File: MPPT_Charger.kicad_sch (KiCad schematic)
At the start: 124 parts, among them J1 Solar, J2 Battery, J4 INTERFACE PORT, J6 JTAG/KEYS, J8 Micro_SD_Card_Det_Hirose_DM3AT, J9 IIC RTC, P1 USB_C_Receptacle_USB2.0_16P, Q1 CSD19505KCS, Q2 CSD19505KCS, Q3 CSD19505KCS, Q4 Si2306, Q5 MMBT3904 1A, Q6 MMBT3904 1A, Q7 Si2306, U1 ACS712, U10 ADS1015, U2 B1212S, U3 AMS1117-5.0, U4 AMS1117-3.3, U5 XL7005A, U6 XL7005A, U7 IR2104, U8 ESP32, U9 CH340G

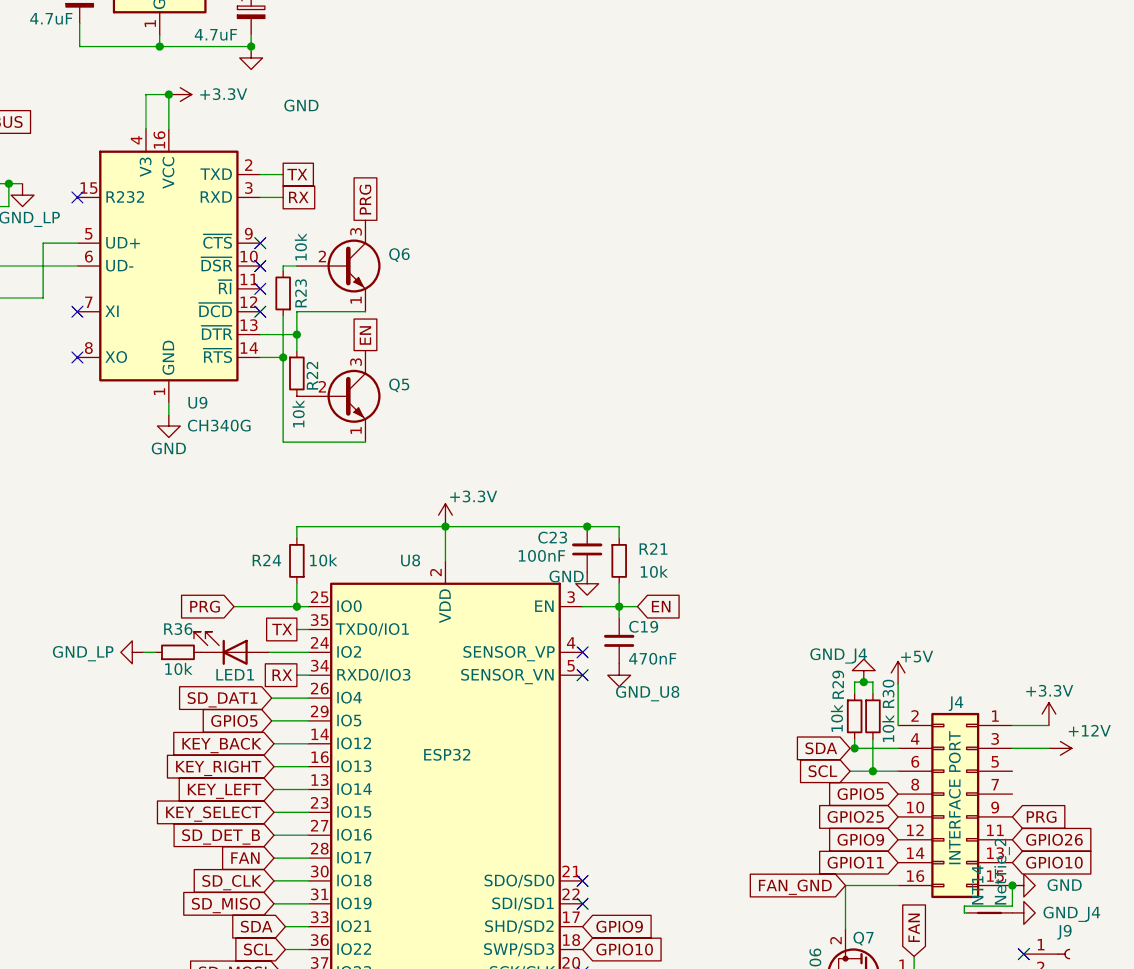
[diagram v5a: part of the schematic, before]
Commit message: RxD TxD were wrong :-(
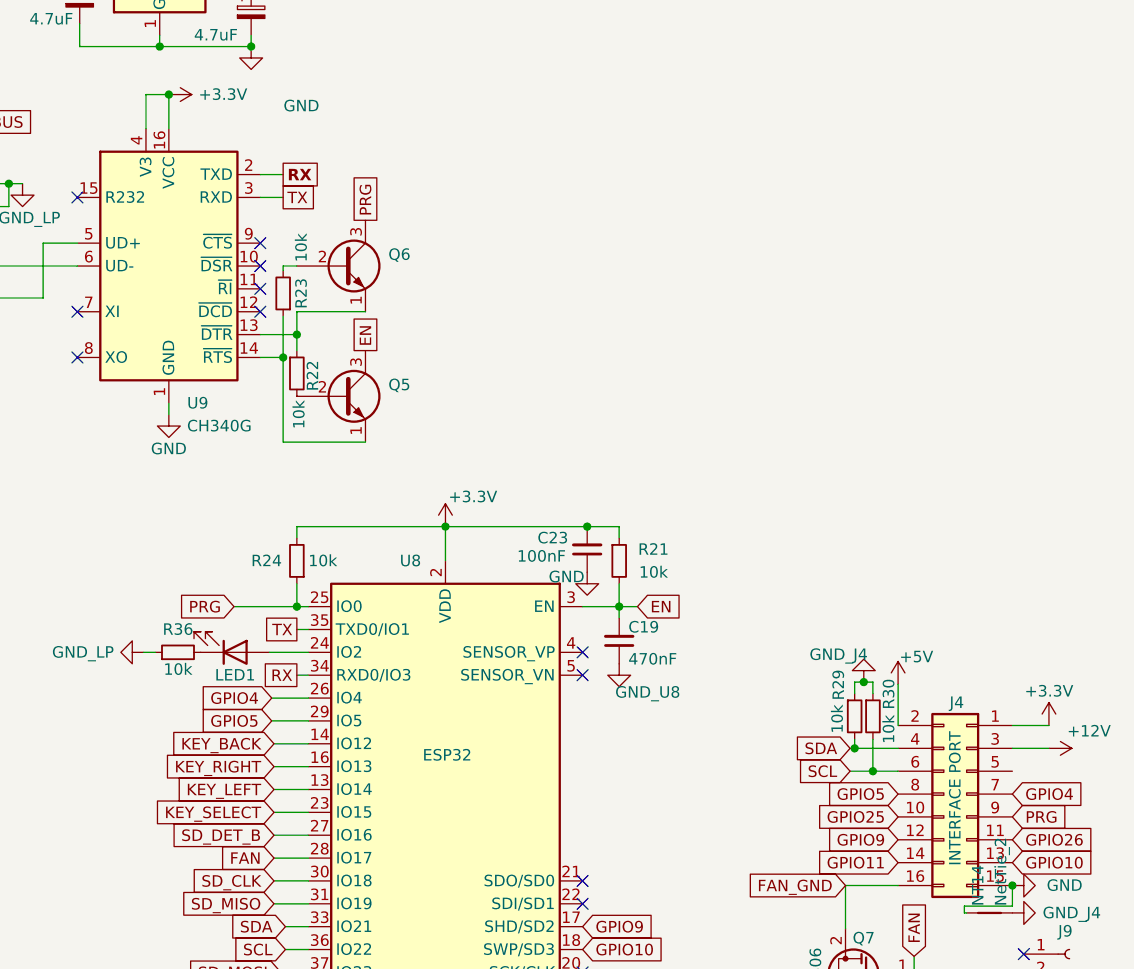
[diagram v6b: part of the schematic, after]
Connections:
- net SD_DAT1 is gone; now on net GPIO4: U8.26 (IO4)
- net RX: now also U9.2 (TXD); no longer U9.3 (RXD)
- net TX: now also U9.3 (RXD); no longer U9.2 (TXD)
- net GPIO4: now reaches J4.7 (Pin_7)
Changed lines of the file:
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@@
-		)
-	)
-	(global_label "SD_DAT1"
-		(shape input)
-		(at 190.246 102.87 180)
-		(fields_autoplaced yes)
-		(effects
-			(font
-				(size 1.27 1.27)
-			)
-			(justify right)
-		)
-		(property "Intersheetrefs" "${INTERSHEET_REFS}"
-			(at 179.85 102.7906 0)
-			(effects
-				(font
-					(size 1.27 1.27)
-				)
-				(justify right)
-				(hide yes)
-			)
 		)
 	)
@@
 		)
 	)
-	(global_label "RX"
+	(global_label "TX"
 		(shape passive)
 		(at 191.516 47.244 0)
@@
 		)
 		(property "Intersheetrefs" "${INTERSHEET_REFS}"
-			(at 196.4086 47.1646 0)
+			(at 195.567 47.244 0)
 			(effects
 				(font
@@
 		)
 	)
-	(global_label "TX"
+	(global_label "RX"
 		(shape passive)
 		(at 191.516 44.704 0)
@@
 			(font
 				(size 1.27 1.27)
-			)
-			(justify left)
-		)
-		(property "Intersheetrefs" "${INTERSHEET_REFS}"
-			(at 196.1062 44.6246 0)
+				(thickness 0.254)
+				(bold yes)
+			)
+			(justify left)
+		)
+		(property "Intersheetrefs" "${INTERSHEET_REFS}"
+			(at 196.3454 44.704 0)
 			(effects
 				(font
@@
 		)
 	)
+	(global_label "GPIO4"
+		(shape input)
+		(at 272.542 113.538 0)
+		(fields_autoplaced yes)
+		(effects
+			(font
+				(size 1.27 1.27)
+			)
+			(justify left)
+		)
+		(property "Intersheetrefs" "${INTERSHEET_REFS}"
+			(at 281.212 113.538 0)
+			(effects
+				(font
+					(size 1.27 1.27)
+				)
+				(justify left)
+				(hide yes)
+			)
+		)
+	)
 	(global_label "SD_MOSI"
 		(shape input)
@@
 				(hide yes)
 			)
+		)
+	)
+	(global_label "GPIO4"
+		(shape input)
+		(at 190.246 102.87 180)
+		(fields_autoplaced yes)
+		(effects
+			(font
+				(size 1.27 1.27)
+			)
+			(justify right)
+		)
+		(property "Intersheetrefs" "${INTERSHEET_REFS}"
+			(at 181.576 102.87 0)
+			(effects
+				(font
+					(size 1.27 1.27)
+				)
+				(justify right)
+				(hide yes)
+			)

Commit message: Kicad 9.0 + minor changes (some "power" vias)
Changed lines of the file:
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@@
 (kicad_sch
-	(version 20231120)
+	(version 20250114)
 	(generator "eeschema")
-	(generator_version "8.0")
+	(generator_version "9.0")
 	(paper "A4")
 	(bus_alias "+3.3V"
 		(members)
 	)
+	(text "EXTERNAL 12-BIT ADC"
+		(exclude_from_sim no)
+		(at 81.534 15.24 0)
+		(effects
+			(font
+				(size 1.27 1.27)
+			)
+			(justify left bottom)
+		)
+	)
+	(text "12V BUCK REGULATOR"
+		(exclude_from_sim no)
+		(at 33.02 43.434 0)
+		(effects
+			(font
+				(size 1.27 1.27)
+			)
+			(justify left bottom)
+		)
+	)
+	(text "BACKFLOW CURRENT CONTROL UNIT\n(BCCU)"
+		(exclude_from_sim no)
+		(at 70.612 74.93 0)
+		(effects
+			(font
+				(size 1.27 1.27)
+			)
+			(justify left bottom)
+		)
+	)
+	(text "USB-TTL UART (ESP 32 USB PROGRAMMER)"
+		(exclude_from_sim no)
+		(at 160.528 17.78 0)
+		(effects
+			(font
+				(size 1.27 1.27)
+			)
+			(justify left bottom)
+		)
+	)
+	(text "3.3V BUCK REGULATOR"
+		(exclude_from_sim no)
+		(at 30.734 16.51 0)
+		(effects
+			(font
+				(size 1.27 1.27)
+			)
+			(justify left bottom)
+		)
+	)
+	(text "5V REGULATOR"
+		(exclude_from_sim no)
+		(at 70.612 42.164 0)
+		(effects
+			(font
+				(size 1.27 1.27)
+			)
+			(justify left bottom)
+		)
+	)
+	(text "MOS DRIVER\n(BUCK DRIVER)"
+		(exclude_from_sim no)
+		(at 55.88 136.144 0)
+		(effects
+			(font
+				(size 1.27 1.27)
+			)
+			(justify left bottom)
+		)
+	)
+	(text "INPUT CURRENT SENSOR"
+		(exclude_from_sim no)
+		(at 34.29 102.362 0)
+		(effects
+			(font
+				(size 1.27 1.27)
+			)
+			(justify left bottom)
+		)
+	)
+	(text "INPUT\nVOLTAGE\nDIVIDER"
+		(exclude_from_sim no)
+		(at 31.75 124.206 0)
+		(effects
+			(font
+				(size 1.27 1.27)
+			)
+			(justify left bottom)
+		)
+	)
 	(junction
 		(at 55.118 139.192)
@@
 		)
 	)
-	(text "EXTERNAL 12-BIT ADC"
-		(exclude_from_sim no)
-		(at 81.534 15.24 0)
-		(effects
-			(font
-				(size 1.27 1.27)
-			)
-			(justify left bottom)
-		)
-	)
-	(text "12V BUCK REGULATOR"
-		(exclude_from_sim no)
-		(at 33.02 43.434 0)
-		(effects
-			(font
-				(size 1.27 1.27)
-			)
-			(justify left bottom)
-		)
-	)
-	(text "BACKFLOW CURRENT CONTROL UNIT\n(BCCU)"
-		(exclude_from_sim no)
-		(at 70.612 74.93 0)
-		(effects
-			(font
-				(size 1.27 1.27)
-			)
-			(justify left bottom)
-		)
-	)
-	(text "USB-TTL UART (ESP 32 USB PROGRAMMER)"
-		(exclude_from_sim no)
-		(at 160.528 17.78 0)
-		(effects
-			(font
-				(size 1.27 1.27)
-			)
-			(justify left bottom)
-		)
-	)
-	(text "3.3V BUCK REGULATOR"
-		(exclude_from_sim no)
-		(at 30.734 16.51 0)
-		(effects
-			(font
-				(size 1.27 1.27)
-			)
-			(justify left bottom)
-		)
-	)
-	(text "5V REGULATOR"
-		(exclude_from_sim no)
-		(at 70.612 42.164 0)
-		(effects
-			(font
-				(size 1.27 1.27)
-			)
-			(justify left bottom)
-		)
-	)
-	(text "MOS DRIVER\n(BUCK DRIVER)"
-		(exclude_from_sim no)
-		(at 55.88 136.144 0)
-		(effects
-			(font
-				(size 1.27 1.27)
-			)
-			(justify left bottom)
-		)
-	)
-	(text "INPUT CURRENT SENSOR"
-		(exclude_from_sim no)
-		(at 34.29 102.362 0)
-		(effects
-			(font
-				(size 1.27 1.27)
-			)
-			(justify left bottom)
-		)
-	)
-	(text "INPUT\nVOLTAGE\nDIVIDER"
-		(exclude_from_sim no)
-		(at 31.75 124.206 0)
-		(effects
-			(font
-				(size 1.27 1.27)
-			)
-			(justify left bottom)
-		)
-	)
 	(global_label "SDA"
 		(shape input)
@@
 		(shape input)
 		(at 258.826 157.226 0)
-		(fields_autoplaced yes)
 		(effects
 			(font
@@
 		(shape input)
 		(at 258.826 152.146 0)
-		(fields_autoplaced yes)
 		(effects
 			(font
@@
 		(shape input)
 		(at 258.826 154.686 0)
-		(fields_autoplaced yes)
 		(effects
 			(font
@@
 		(shape input)
 		(at 258.826 149.606 0)
-		(fields_autoplaced yes)
 		(effects
 			(font
@@
 		(exclude_from_sim no)
 		(in_bom no)
-		(on_board yes)
+		(on_board no)
 		(dnp no)
 		(property "Reference" "NT5"
@@
 		)
 	)
+	(embedded_fonts no)
 )
